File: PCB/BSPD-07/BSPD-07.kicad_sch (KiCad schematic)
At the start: 60 parts, among them IC1 LM393LVQDRQ1, IC2 LM393LVQDRQ1, IC3 LM393LVQDRQ1, IC4 LDO40LPU50RY, IC5 74LVC1G02GW-Q100H, IC6 LM393LVQDRQ1, J1 DTM13-12PA, Q1 RSQ025P03HZGTR, Q2 RJU002N06FRAT106, Q3 RJU002N06FRAT106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

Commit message: WIP layouting SCS section
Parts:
- added R29: 200, Resistor_SMD:R_0402_1005Metric, symbol Device:R_Small
- added R30: 10k, Resistor_SMD:R_0402_1005Metric, symbol Device:R_Small
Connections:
- net +5V: now also R29.2
- net GND: now also R30.1
- net at IC6.3 (IN1+), R18.2, R27.1: no longer IC6.5 (IN2+)
- new net: IC6.5 (IN2+), R29.1, R30.2
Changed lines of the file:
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@@
   (junction (at 50.8 97.79) (diameter 0) (color 0 0 0 0)
   )
-  (junction (at 43.815 153.035) (diameter 0) (color 0 0 0 0)
-  )
   (junction (at 105.41 41.91) (diameter 0) (color 0 0 0 0)
   )
@@
   (junction (at 41.91 40.64) (diameter 0) (color 0 0 0 0)
   )
+  (junction (at 43.815 160.655) (diameter 0) (color 0 0 0 0)
+  )
   (junction (at 36.83 100.33) (diameter 0) (color 0 0 0 0)
   )
@@
     (stroke (width 0) (type default) (color 0 0 0 0))
   )
-  (wire (pts (xy 43.815 153.035) (xy 59.69 153.035))
+  (wire (pts (xy 41.275 153.035) (xy 59.69 153.035))
+    (stroke (width 0) (type default) (color 0 0 0 0))
+  )
+  (wire (pts (xy 36.195 160.655) (xy 34.29 160.655))
+    (stroke (width 0) (type default) (color 0 0 0 0))
+  )
+  (wire (pts (xy 43.815 160.655) (xy 41.275 160.655))
     (stroke (width 0) (type default) (color 0 0 0 0))
   )
@@
     (stroke (width 0) (type default) (color 0 0 0 0))
   )
+  (wire (pts (xy 43.815 163.195) (xy 43.815 160.655))
+    (stroke (width 0) (type default) (color 0 0 0 0))
+  )
   (wire (pts (xy 56.515 204.47) (xy 56.515 205.74))
     (stroke (width 0) (type default) (color 0 0 0 0))
@@
     (stroke (width 0) (type default) (color 0 0 0 0))
   )
-  (wire (pts (xy 41.275 153.035) (xy 43.815 153.035))
-    (stroke (width 0) (type default) (color 0 0 0 0))
-  )
   (wire (pts (xy 213.36 67.31) (xy 256.54 67.31))
     (stroke (width 0) (type default) (color 0 0 0 0))
@@
     (stroke (width 0) (type default) (color 0 0 0 0))
   )
-  (wire (pts (xy 43.815 160.655) (xy 43.815 153.035))
-    (stroke (width 0) (type default) (color 0 0 0 0))
-  )
   (polyline (pts (xy 270.51 44.45) (xy 270.51 77.47))
     (stroke (width 0) (type default) (color 0 0 0 0))
@@
     (effects (font (size 1.27 1.27)) (justify left bottom))
   )
+  (text "~4.9V" (at 50.8 153.035 0)
+    (effects (font (size 1.27 1.27)) (justify left bottom))
+  )
   (text "ERR = LOW" (at 79.375 181.61 0)
     (effects (font (size 2 2)) (justify left bottom))
@@
     (effects (font (size 1.8 1.8) italic) (justify left bottom))
   )
-  (text "~4.9V" (at 38.1 156.845 0)
+  (text "~4.9V" (at 50.8 160.655 0)
     (effects (font (size 1.27 1.27)) (justify left bottom))
   )
@@
     (pin "1")
   )
+  (symbol (lib_id "Device:R_Small") (at 38.735 160.655 270) (mirror x) (unit 1)
+    (in_bom yes) (on_board yes)
+    (property "Reference" "R29" (id 0) (at 37.465 156.21 0)
+      (effects (font (size 1.27 1.27)) (justify right))
+    )
+    (property "Value" "200" (id 1) (at 40.005 154.94 0)
+      (effects (font (size 1.27 1.27)) (justify right))
+    )
+    (property "Footprint" "Resistor_SMD:R_0402_1005Metric" (id 2) (at 38.735 160.655 0)
+      (effects (font (size 1.27 1.27)) hide)
+    )
+    (property "Datasheet" "~" (id 3) (at 38.735 160.655 0)
+      (effects (font (size 1.27 1.27)) hide)
+    )
+    (pin "1")
+    (pin "2")
+  )
   (symbol (lib_id "Device:C_Small") (at 221.615 118.745 0) (unit 1)
     (in_bom yes) (on_board yes)
@@
     (pin "2")
   )
+  (symbol (lib_id "Device:R_Small") (at 43.815 165.735 0) (mirror x) (unit 1)
+    (in_bom yes) (on_board yes)
+    (property "Reference" "R30" (id 0) (at 41.275 165.735 90))
+    (property "Value" "10k" (id 1) (at 39.37 165.735 90))
+    (property "Footprint" "Resistor_SMD:R_0402_1005Metric" (id 2) (at 43.815 165.735 0)
+      (effects (font (size 1.27 1.27)) hide)
+    )
+    (property "Datasheet" "~" (id 3) (at 43.815 165.735 0)
+      (effects (font (size 1.27 1.27)) hide)
+    )
+    (pin "1")
+    (pin "2")
+  )
   (symbol (lib_id "Device:C_Small") (at 267.335 118.745 0) (unit 1)
     (in_bom yes) (on_board yes)
@@
     (pin "2")
   )
+  (symbol (lib_id "power:GND") (at 43.815 168.275 0) (mirror y) (unit 1)
+    (in_bom yes) (on_board yes)
+    (property "Reference" "#PWR0158" (id 0) (at 43.815 174.625 0)
+      (effects (font (size 1.27 1.27)) hide)
+    )
+    (property "Value" "GND" (id 1) (at 41.91 172.085 0)
+      (effects (font (size 1.27 1.27)) (justify right))
+    )
+    (property "Footprint" "" (id 2) (at 43.815 168.275 0)
+      (effects (font (size 1.27 1.27)) hide)
+    )
+    (property "Datasheet" "" (id 3) (at 43.815 168.275 0)
+      (effects (font (size 1.27 1.27)) hide)
+    )
+    (pin "1")
+  )
   (symbol (lib_id "power:+5V") (at 91.44 95.25 270) (unit 1)
     (in_bom yes) (on_board yes) (fields_autoplaced)
@@
     (pin "1")
   )
+  (symbol (lib_id "power:+5V") (at 34.29 160.655 90) (mirror x) (unit 1)
+    (in_bom yes) (on_board yes) (fields_autoplaced)
+    (property "Reference" "#PWR0157" (id 0) (at 38.1 160.655 0)
+      (effects (font (size 1.27 1.27)) hide)
+    )
+    (property "Value" "+5V" (id 1) (at 29.845 160.655 0))
+    (property "Footprint" "" (id 2) (at 34.29 160.655 0)
+      (effects (font (size 1.27 1.27)) hide)
+    )
+    (property "Datasheet" "" (id 3) (at 34.29 160.655 0)
+      (effects (font (size 1.27 1.27)) hide)
+    )
+    (pin "1")
+  )
   (symbol (lib_id "power:GND") (at 212.09 29.845 180) (unit 1)
     (in_bom yes) (on_board yes) (fields_autoplaced)
@@
       (reference "#PWR0156") (unit 1) (value "+5V") (footprint "")
     )
+    (path "/f6fc89ed-09d1-4c71-97fd-1ac7047d11e8"
+      (reference "#PWR0157") (unit 1) (value "+5V") (footprint "")
+    )
+    (path "/59bdbfe9-3713-4f1e-9490-af2f1860b3ff"
+      (reference "#PWR0158") (unit 1) (value "GND") (footprint "")
+    )
     (path "/118f0778-e9d3-4271-8bcc-a274169adaa4"
       (reference "C1") (unit 1) (value "0.1uF") (footprint "Capacitor_SMD:C_0402_1005Metric")
@@
       (reference "R28") (unit 1) (value "100") (footprint "Resistor_SMD:R_0402_1005Metric")
     )
+    (path "/2dc695f4-21ec-4e69-896a-8a48e4bc7ba4"
+      (reference "R29") (unit 1) (value "200") (footprint "Resistor_SMD:R_0402_1005Metric")
+    )
+    (path "/4bbe9407-c358-42d2-b2ca-9969afde8412"
+      (reference "R30") (unit 1) (value "10k") (footprint "Resistor_SMD:R_0402_1005Metric")
+    )
     (path "/75a97f9d-2bc2-44fe-8866-ca67331262e0"

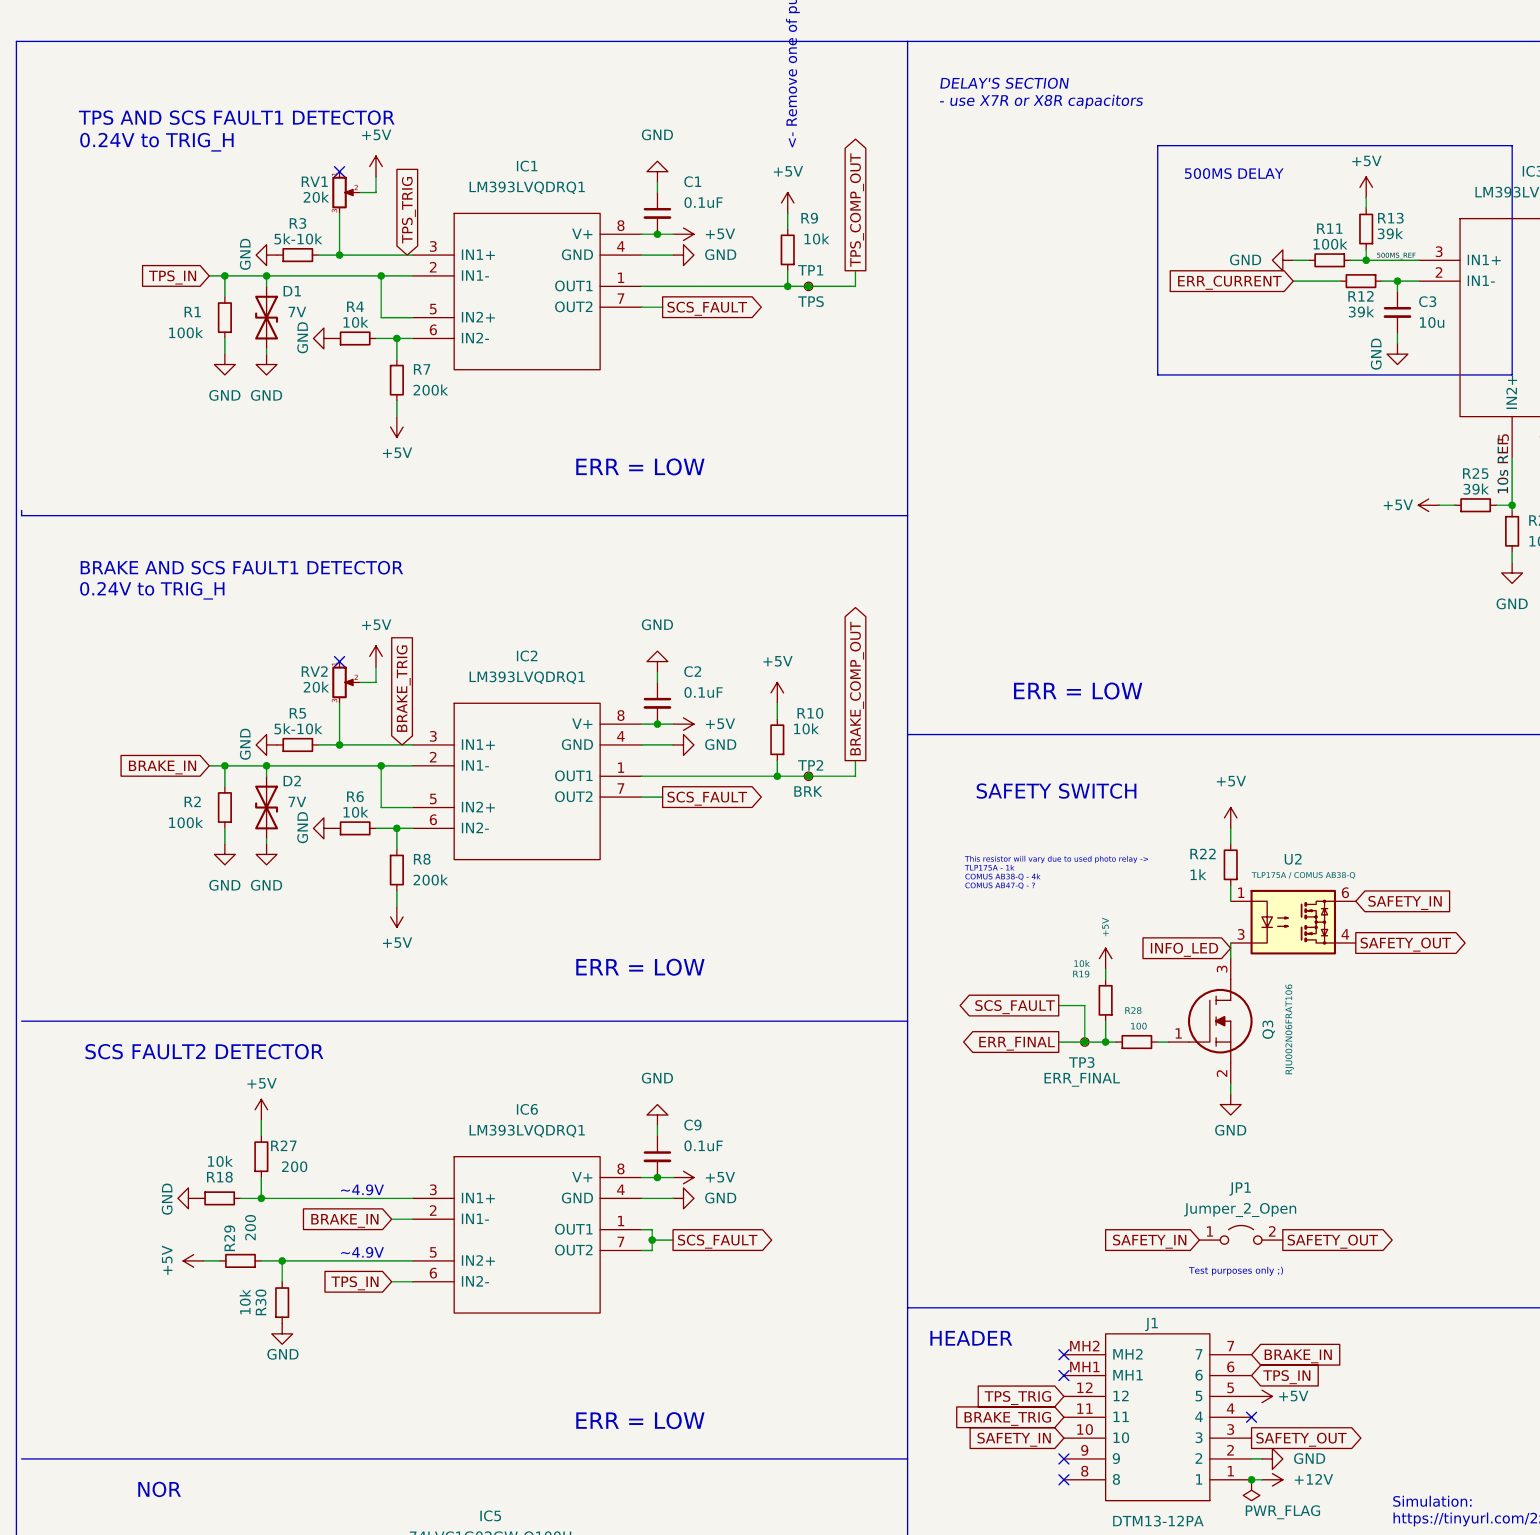
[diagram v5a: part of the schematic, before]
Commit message: New layout for 2024 - scs compliance
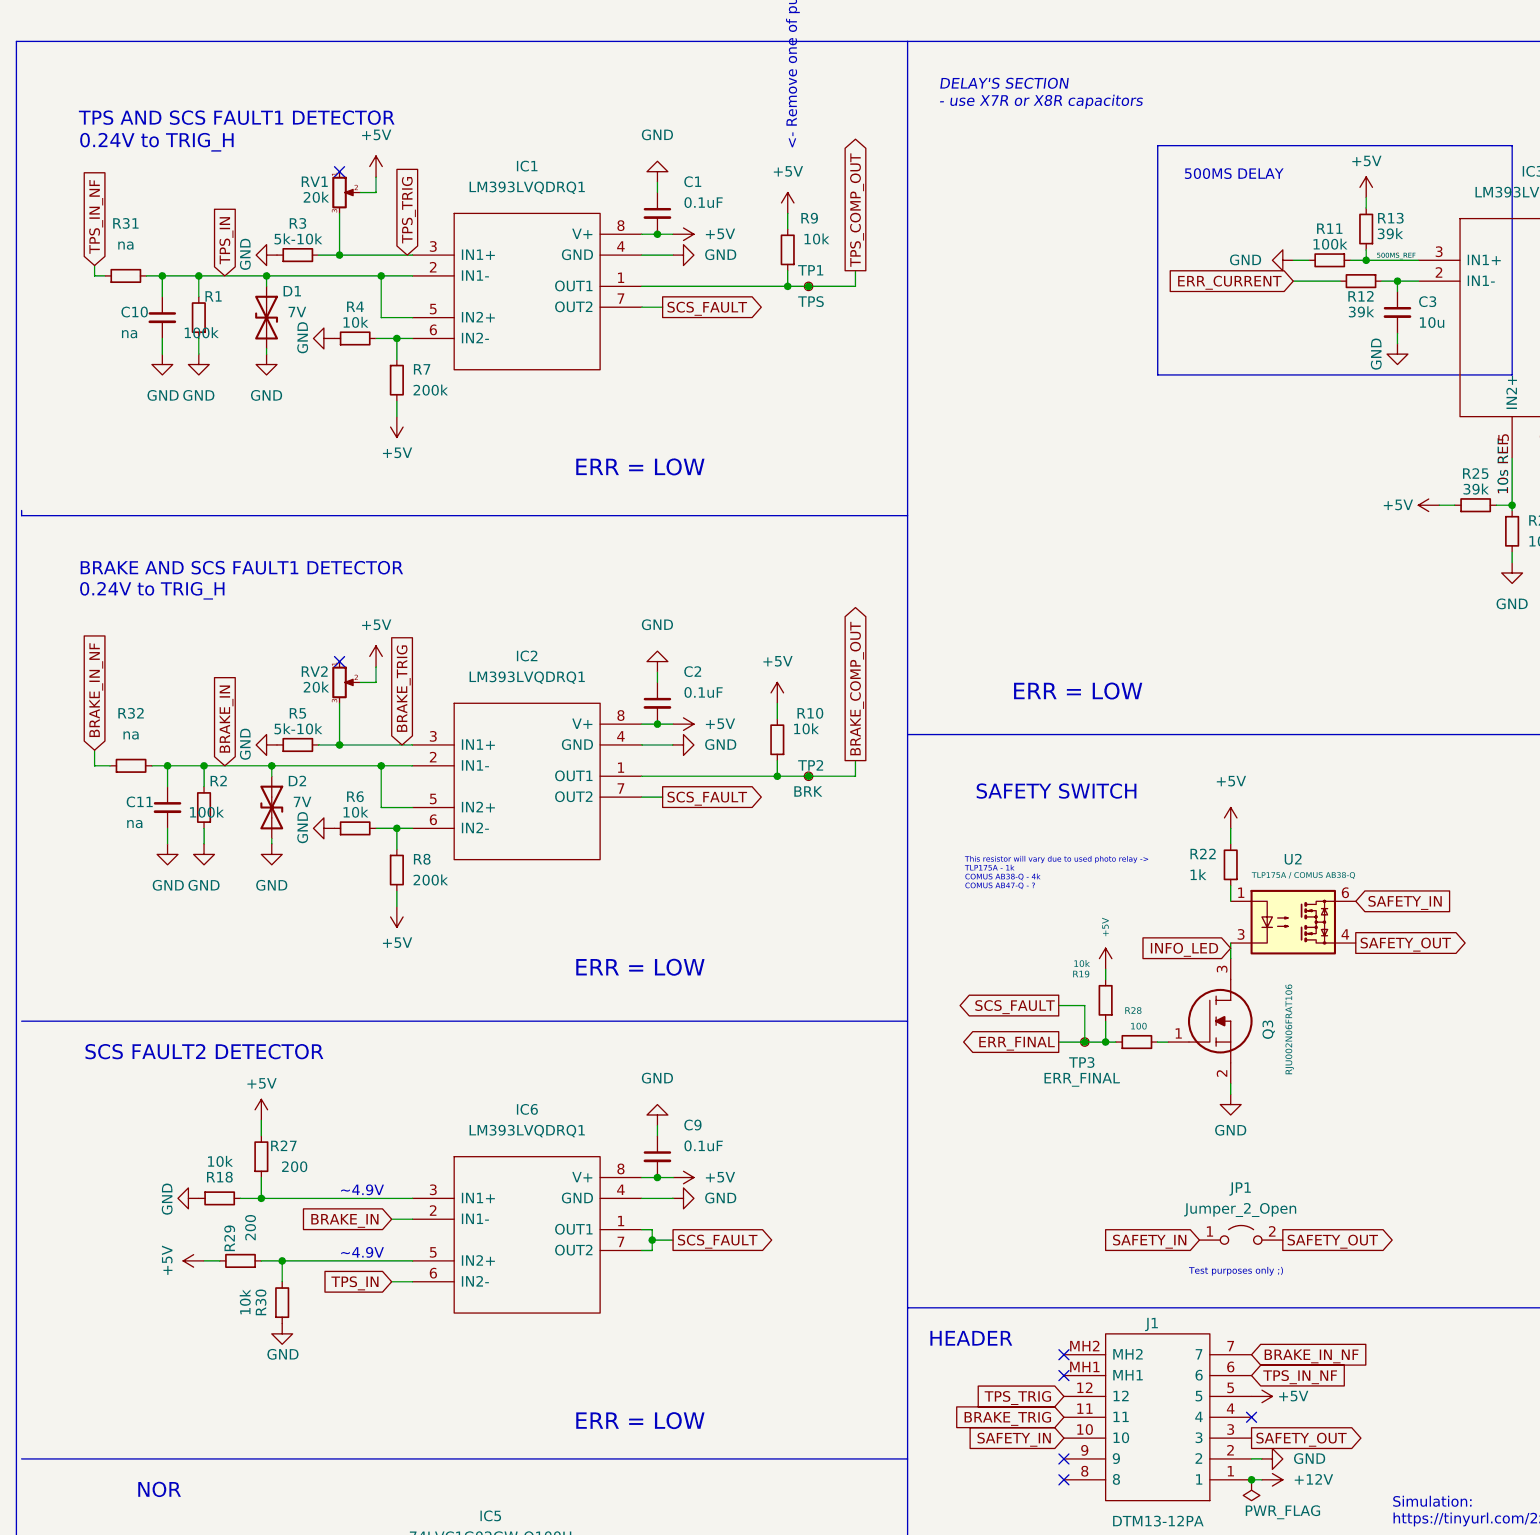
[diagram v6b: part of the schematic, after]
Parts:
- added C10, C11: na, Capacitor_SMD:C_0402_1005Metric, symbol Device:C_Small
- added R31, R32: na, Resistor_SMD:R_0402_1005Metric, symbol Device:R_Small
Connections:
- net BRAKE_IN: now also C11.1, R32.2; no longer J1.7
- net GND: now also C10.2, C11.2
- net TPS_IN: now also C10.1, R31.2; no longer J1.6
- new net BRAKE_IN_NF: J1.7, R32.1
- new net TPS_IN_NF: J1.6, R31.1
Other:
- moved on the sheet: D2, R1, R2

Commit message: Added adnotations during soldering
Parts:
- R14: value 5 -> 5R2
- R16: value 100 -> 100R
- R21: value 2-4 -> 3R9
- R27: value 200 -> 200R
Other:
- note added: "LPF: R31 + C10 R32 + C11 1k2 + 1uF ~ 130 Hz cut-off"
- note added: "NOW: CPC1017N"
- note added: "R3, R5 Currently: 6k33 Will be: 6k2"
- note added: "This resistor will vary due to used photo relay -> TLP175A - 1k COMUS AB38-Q - 4k COMUS AB47-Q - ? CPC1017N - 1k"
- note added: "Wlutowane 3R9"
- note added: "Wlutowane 5R2"
- note removed: "This resistor will vary due to used photo relay -> TLP175A - 1k COMUS AB38-Q - 4k COMUS AB47-Q - ?"
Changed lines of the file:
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@@
+    (effects (font (size 1.27 1.27)) (justify left bottom))
+  )
+  (text "R3, R5 Currently: 6k33\nWill be: 6k2" (at 26.797 30.48 0)
     (effects (font (size 1.27 1.27)) (justify left bottom))
   )
@@
     (effects (font (size 2 2)) (justify left bottom))
   )
+  (text "Wlutowane 5R2\n\n" (at 236.728 60.96 0)
+    (effects (font (size 1.27 1.27)) (justify left bottom))
+  )
   (text "Discharging capacitor when implausibility occurs" (at 231.775 32.385 0)
     (effects (font (size 1 1)) (justify left bottom))
   )
-  (text "This resistor will vary due to used photo relay ->\nTLP175A - 1k\nCOMUS AB38-Q - 4k\nCOMUS AB47-Q - ?"
+  (text "This resistor will vary due to used photo relay ->\nTLP175A - 1k\nCOMUS AB38-Q - 4k\nCOMUS AB47-Q - ?\nCPC1017N - 1k"
     (at 127 115.57 0)
     (effects (font (size 0.67 0.67)) (justify left bottom))
   )
+  (text "NOW: CPC1017N" (at 160.909 125.603 0)
+    (effects (font (size 1.27 1.27)) (justify left bottom))
+  )
+  (text "LPF:\nR31 + C10\nR32 + C11\n1k2 + 1uF ~ 130 Hz cut-off"
+    (at 15.113 66.167 0)
+    (effects (font (size 1.27 1.27) italic) (justify left bottom))
+  )
   (text "Test purposes only ;)" (at 154.305 162.56 0)
     (effects (font (size 0.8 0.8)) (justify left bottom))
@@
   )
   (text "<- Currently 1.1M" (at 274.32 68.58 0)
+    (effects (font (size 1.27 1.27)) (justify left bottom))
+  )
+  (text "Wlutowane 3R9" (at 232.156 69.596 0)
     (effects (font (size 1.27 1.27)) (justify left bottom))
   )
@@
   (symbol (lib_id "Device:R_Small") (at 218.44 42.545 90) (unit 1)
     (in_bom yes) (on_board yes)
-    (property "Reference" "R16" (id 0) (at 217.17 40.64 90)
-      (effects (font (size 0.8 0.8)))
-    )
-    (property "Value" "100" (id 1) (at 219.71 40.64 90)
-      (effects (font (size 0.8 0.8)))
-    )
+    (property "Reference" "R16" (id 0) (at 218.313 40.767 90))
+    (property "Value" "100R" (id 1) (at 218.186 44.831 90))
     (property "Footprint" "Resistor_SMD:R_0402_1005Metric" (id 2) (at 218.44 42.545 0)
       (effects (font (size 1.27 1.27)) hide)
@@
       (effects (font (size 1.27 1.27)) (justify left))
     )
-    (property "Value" "5" (id 1) (at 252.73 59.055 0)
+    (property "Value" "5R2" (id 1) (at 251.46 59.817 0)
       (effects (font (size 1.27 1.27)) (justify left))
     )
@@
   (symbol (lib_id "Device:R_Small") (at 238.76 78.74 270) (unit 1)
     (in_bom yes) (on_board yes)
-    (property "Reference" "R21" (id 0) (at 238.125 71.755 90))
-    (property "Value" "2-4" (id 1) (at 238.76 74.93 90))
+    (property "Reference" "R21" (id 0) (at 239.268 74.803 90))
+    (property "Value" "3R9" (id 1) (at 239.268 76.708 90))
     (property "Footprint" "Resistor_SMD:R_0402_1005Metric" (id 2) (at 238.76 78.74 0)
       (effects (font (size 1.27 1.27)) hide)
@@
   (symbol (lib_id "Device:R_Small") (at 41.275 147.955 0) (mirror x) (unit 1)
     (in_bom yes) (on_board yes)
-    (property "Reference" "R27" (id 0) (at 45.72 146.685 0)
-      (effects (font (size 1.27 1.27)) (justify right))
-    )
-    (property "Value" "200" (id 1) (at 46.99 149.225 0)
+    (property "Reference" "R27" (id 0) (at 46.355 146.812 0)
+      (effects (font (size 1.27 1.27)) (justify right))
+    )
+    (property "Value" "200R" (id 1) (at 48.006 149.225 0)
       (effects (font (size 1.27 1.27)) (justify right))
     )
@@
     )
     (path "/7f467454-440b-4835-9c3b-fbc2452c38ab"
-      (reference "R14") (unit 1) (value "5") (footprint "Resistor_SMD:R_0402_1005Metric")
+      (reference "R14") (unit 1) (value "5R2") (footprint "Resistor_SMD:R_0402_1005Metric")
     )
     (path "/b844dfab-c885-4983-97f0-a2e19271c471"
@@
     )
     (path "/4a40b7c5-bf23-4b2d-8f86-5540cc3a7815"
-      (reference "R16") (unit 1) (value "100") (footprint "Resistor_SMD:R_0402_1005Metric")
+      (reference "R16") (unit 1) (value "100R") (footprint "Resistor_SMD:R_0402_1005Metric")
     )
     (path "/d28202c2-7069-4207-8eb1-248ef409b06f"
@@
     )
     (path "/97b6a835-3d9b-4659-9565-972e7ba6b6ea"
-      (reference "R21") (unit 1) (value "2-4") (footprint "Resistor_SMD:R_0402_1005Metric")
+      (reference "R21") (unit 1) (value "3R9") (footprint "Resistor_SMD:R_0402_1005Metric")
     )
     (path "/2b79b8d1-ca8d-4b8e-a334-4700ba36aa24"
@@
     )
     (path "/e0128100-ca6d-44a4-ba50-42837460a725"
-      (reference "R27") (unit 1) (value "200") (footprint "Resistor_SMD:R_0402_1005Metric")
+      (reference "R27") (unit 1) (value "200R") (footprint "Resistor_SMD:R_0402_1005Metric")
     )
     (path "/88d73622-8494-48e9-aefa-364e7085331e"

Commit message: Minor changes after assembly
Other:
- note added: "NOW: 750R0"
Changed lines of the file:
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@@
     (effects (font (size 1.8 1.8)) (justify left bottom))
+  )
+  (text "NOW: 750R0" (at 163.957 217.297 0)
+    (effects (font (size 1.27 1.27)) (justify left bottom))
   )
   (text "LDO" (at 212.09 104.14 0)
